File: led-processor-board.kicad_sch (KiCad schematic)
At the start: 66 parts, among them J1 10103594-0001LF, J2 SPARE, J3 SWD, SW1 434133025816, SW2 434133025816, U1 RP2350B, U2 NCP1117ST33T3G, U3 W25Q128JVSIQ, U4 APS6404L-3SQR-SN, U5 RM2, U6 DS3231SN, X1 12MHz

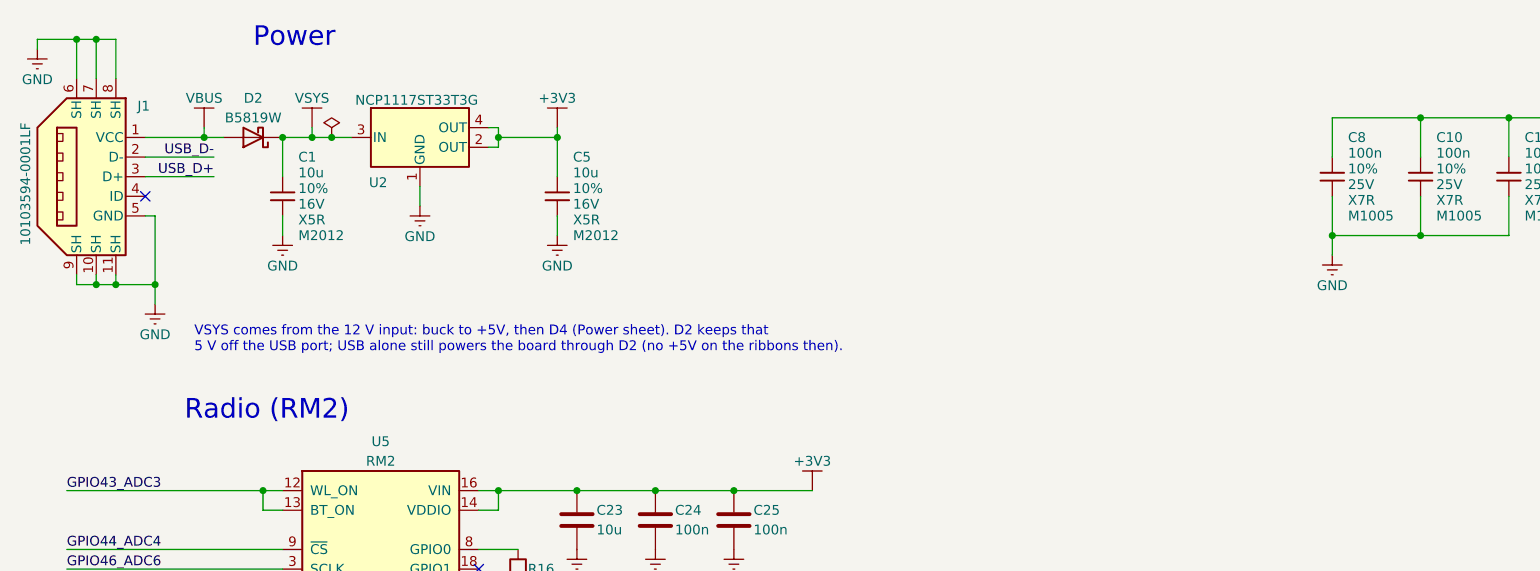
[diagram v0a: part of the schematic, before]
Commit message: Use a USB-C receptacle instead of the micro-B
J1 is now a Korean Hroparts TYPE-C-31-M-12 (LCSC C165948, stock KiCad
footprint), USB 2.0: D+/D- from both sides joined, 5.1k pull-downs on
CC1/CC2 (R56, R57), SBU unconnected, shell to GND. VBUS still feeds D2.
PWR_FLAGs on VBUS and GND replace the drive the old symbol's power pins
gave; ERC is unchanged (only Pi's inherited items).

Co-Authored-By: Claude Opus 5.5 (1M context) <noreply@anthropic.com>
Claude-Session: https://claude.ai/code/session_01CYnkeL97vxsPSCyXSKGro9
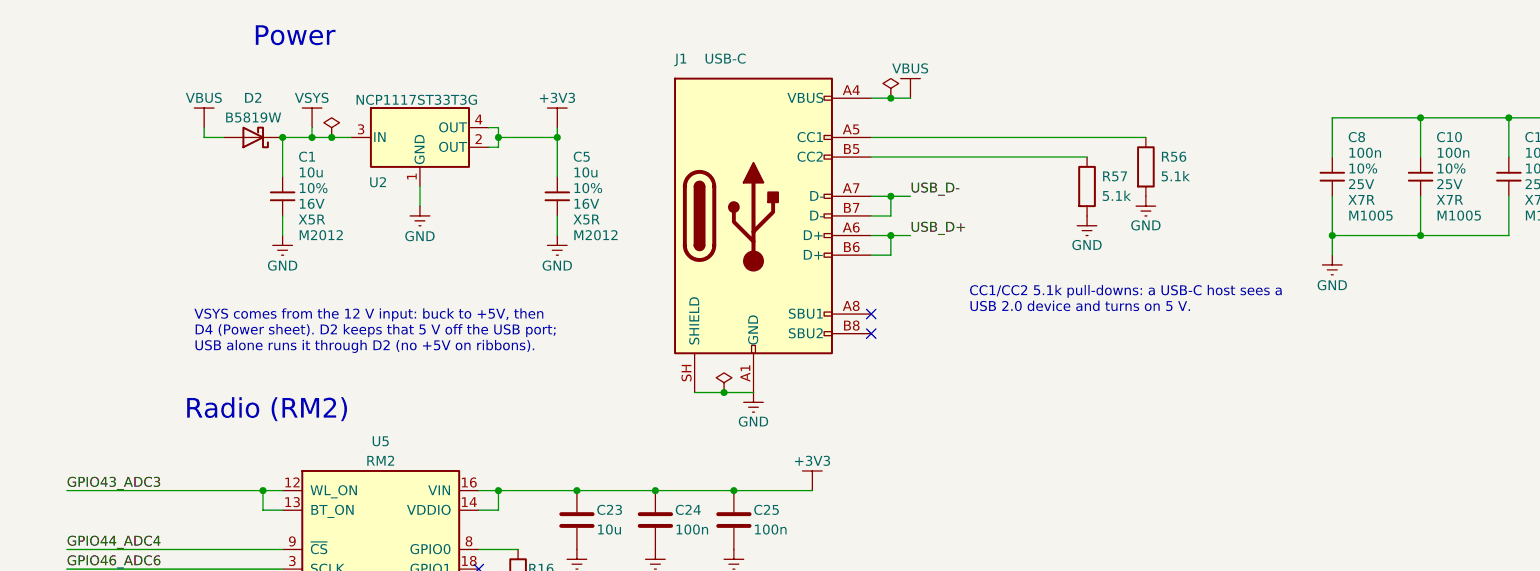
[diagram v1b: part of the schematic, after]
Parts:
- removed J1: 10103594-0001LF, RPI_COMPILED:amphenol_10103594-0001lf, symbol RPI_DB:Connectors | USB/RP-019A1P-1JAX7V
- added J1: USB-C, Connector_USB:USB_C_Receptacle_HRO_TYPE-C-31-M-12, symbol Connector:USB_C_Receptacle_USB2.0_16P
- added R56, R57: 5.1k, Resistor_SMD:R_0402_1005Metric, symbol Device:R
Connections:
- net GND: now also J1.A1 (GND), J1.A12 (GND), J1.B1 (GND), J1.B12 (GND), J1.SH (SHIELD), R56.2, R57.2
- net USB_D+: now also J1.A6 (D+), J1.B6 (D+)
- net USB_D-: now also J1.A7 (D-), J1.B7 (D-)
- net VBUS: now also J1.A4 (VBUS), J1.A9 (VBUS), J1.B4 (VBUS), J1.B9 (VBUS)
- new net: J1.A5 (CC1), R56.1
- new net: J1.B5 (CC2), R57.1
- no-connect marks 8 -> 9
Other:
- note added: "CC1/CC2 5.1k pull-downs: a USB-C host sees a USB 2.0 device and turns on 5 V."
- note added: "VSYS comes from the 12 V input: buck to +5V, then D4 (Power sheet). D2 keeps that 5 V off the USB port; USB alone runs it through D2 (no +5V on ribbons)."
- note removed: "VSYS comes from the 12 V input: buck to +5V, then D4 (Power sheet). D2 keeps that 5 V off the USB port; USB alone still powers the board through D2 (no +5V on the ribbons then)."

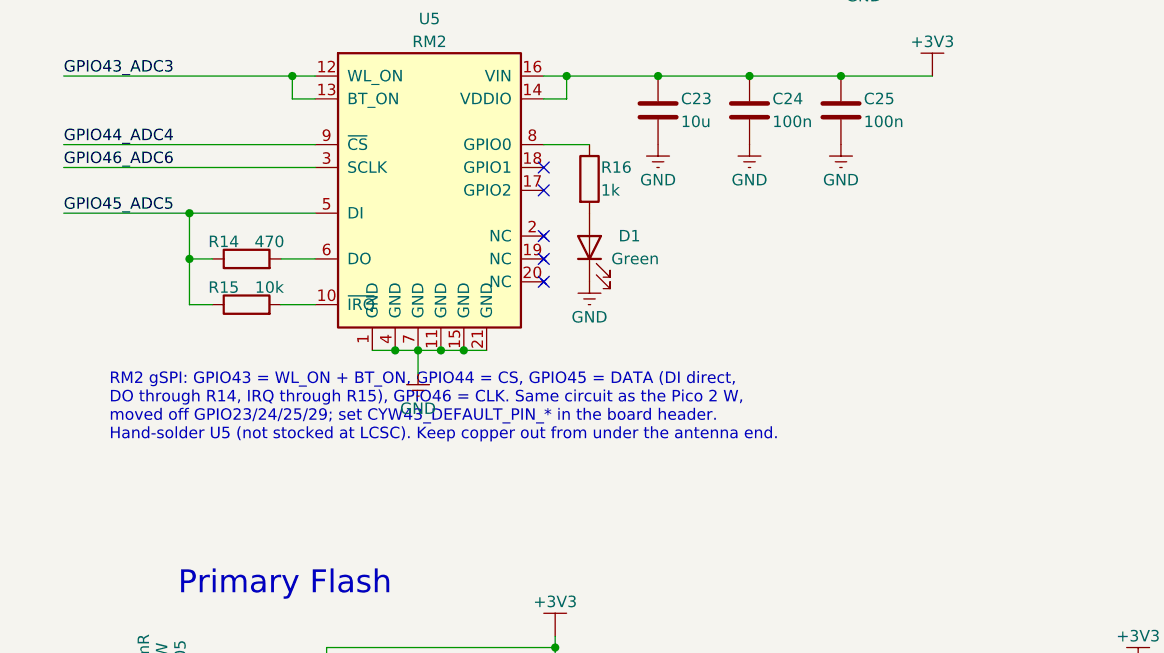
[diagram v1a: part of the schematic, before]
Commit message: Bottom shrouds to the edge; add J9 for the RM2's spare GPIOs
J7/J8 move down until their bottom pins sit just above the antenna
strip, like the left-edge shrouds; J8 also shifts 1.6 mm left to clear
the corner hole. Their 3V3/5V runs are hand-routed through the channel
between the pin rows (one net per layer) and the caps sit above the
shrouds' right ends. This replaces the old OUT4 3V3 run along the
bottom edge into the radio's 3V3 pour.

J9 (1x3: WL_GPIO1, WL_GPIO2, GND) breaks out the CYW43's two unused
GPIOs beside the RM2, in the schematic and on the board; C23/C24 move
up to make room. DRC with schematic parity is clean apart from the
inherited warnings.

Co-Authored-By: Claude Opus 5.5 (1M context) <noreply@anthropic.com>
Claude-Session: https://claude.ai/code/session_01CYnkeL97vxsPSCyXSKGro9
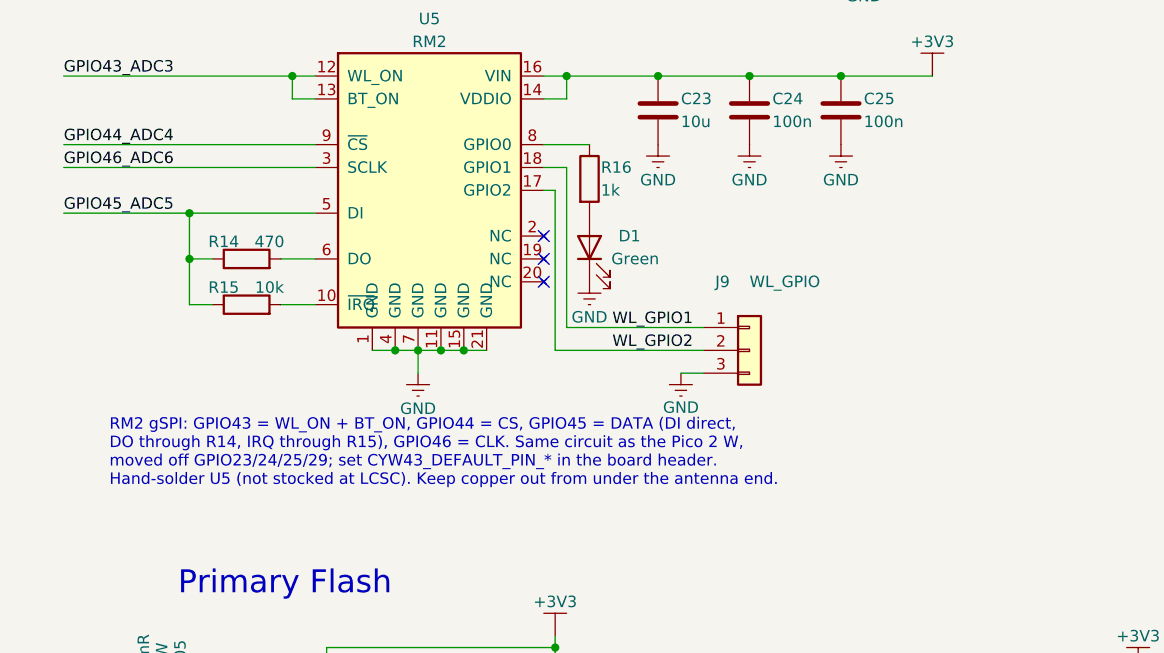
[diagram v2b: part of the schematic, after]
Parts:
- added J9: WL_GPIO, Connector_PinHeader_2.54mm:PinHeader_1x03_P2.54mm_Vertical, symbol Connector_Generic:Conn_01x03
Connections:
- net GND: now also J9.3 (Pin_3)
- net WL_GPIO2: now reaches U5.17 (GPIO2)
- net WL_GPIO2: now also J9.2 (Pin_2)
- net WL_GPIO1: now reaches U5.18 (GPIO1)
- net WL_GPIO1: now also J9.1 (Pin_1)
- no-connect marks 9 -> 7

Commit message: LCSC buttons, and JLCPCB files for SMD-only assembly
SW1/SW2 become the XKB TS-1088R-02526 (LCSC C455281) in Pi's spots, with
the schematic symbols swapped to Switch:SW_Push. tools/jlc.py writes fab/:
gerbers + drill zip, and a BOM and CPL with only the SMD parts JLC places.
The RM2, battery holder, headers, shrouds and J4 are left to hand-solder.

Co-Authored-By: Claude Opus 5.5 (1M context) <noreply@anthropic.com>
Claude-Session: https://claude.ai/code/session_01CYnkeL97vxsPSCyXSKGro9
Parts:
- SW1, SW2: value 434133025816 -> TS-1088R-02526; footprint RPI_COMPILED:wurthelek_434133025816 -> Button_Switch_SMD:SW_SPST_TS-1088-xR025; symbol RPI_DB:Electromechanical | Switches | Tactile/RP-01H0MT-6E9H8F -> Switch:SW_Push; LCSC (none) -> C455281; manufacturer Wurth Elektronik -> XKB Connection; manufacturer_pn 434133025816 -> TS-1088R-02526; package 4.2x3.2x2.5mm -> 4x3x2.5mm; packaging 330mm dia. tape & reel -> (none); packaging_qty 2900 -> (none); part_uid RP-01H0MT-6E9H8F -> (none); size 4.2x3.2x2.5mm -> 4x3x2.5mm
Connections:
- net GND: no longer SW1.2
- net RUN: now also SW2.2; no longer SW2.3, SW2.4
- net ~{USB_BOOT}: now also SW1.2; no longer SW1.3, SW1.4
- net at R4.1, SW2.1: no longer SW2.2
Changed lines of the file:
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@@
 	)
 	(junction
-		(at 265.43 246.38)
-		(diameter 0)
-		(color 0 0 0 0)
-	)
-	(junction
 		(at 304.8 25.4)
 		(diameter 0)
@@
 	)
 	(junction
-		(at 20.32 180.34)
-		(diameter 0)
-		(color 0 0 0 0)
-	)
-	(junction
 		(at 36.83 152.4)
 		(diameter 0)
@@
 	)
 	(junction
-		(at 250.19 246.38)
-		(diameter 0)
-		(color 0 0 0 0)
-	)
-	(junction
 		(at 236.22 101.6)
 		(diameter 0)
@@
 	)
 	(junction
-		(at 20.32 195.58)
-		(diameter 0)
-		(color 0 0 0 0)
-	)
-	(junction
 		(at 207.01 101.6)
 		(diameter 0)
@@
 	(wire
 		(pts
-			(xy 251.46 248.92) (xy 250.19 248.92)
-		)
-		(stroke
-			(width 0)
-			(type default)
-		)
-	)
-	(wire
-		(pts
 			(xy 265.43 129.54) (xy 245.11 129.54)
 		)
@@
 	(wire
 		(pts
-			(xy 265.43 246.38) (xy 264.16 246.38)
+			(xy 265.43 246.38) (xy 262.89 246.38)
 		)
 		(stroke
@@
 	(wire
 		(pts
-			(xy 22.86 180.34) (xy 20.32 180.34)
-		)
-		(stroke
-			(width 0)
-			(type default)
-		)
-	)
-	(wire
-		(pts
 			(xy 49.53 83.82) (xy 21.59 83.82)
 		)
@@
 	(wire
 		(pts
-			(xy 251.46 246.38) (xy 250.19 246.38)
+			(xy 252.73 246.38) (xy 250.19 246.38)
 		)
 		(stroke
@@
 	(wire
 		(pts
-			(xy 265.43 248.92) (xy 265.43 246.38)
-		)
-		(stroke
-			(width 0)
-			(type default)
-		)
-	)
-	(wire
-		(pts
 			(xy 38.1 93.98) (xy 35.56 93.98)
 		)
@@
 	(wire
 		(pts
-			(xy 22.86 194.31) (xy 22.86 195.58)
-		)
-		(stroke
-			(width 0)
-			(type default)
-		)
-	)
-	(wire
-		(pts
 			(xy 50.8 137.16) (xy 50.8 140.97)
 		)
@@
 	(wire
 		(pts
-			(xy 22.86 195.58) (xy 20.32 195.58)
-		)
-		(stroke
-			(width 0)
-			(type default)
-		)
-	)
-	(wire
-		(pts
 			(xy 143.51 245.11) (xy 158.75 245.11)
 		)
@@
 	(wire
 		(pts
-			(xy 250.19 248.92) (xy 250.19 246.38)
-		)
-		(stroke
-			(width 0)
-			(type default)
-		)
-	)
-	(wire
-		(pts
 			(xy 208.28 215.9) (xy 208.28 193.04)
 		)
@@
 	(wire
 		(pts
-			(xy 20.32 180.34) (xy 20.32 181.61)
+			(xy 20.32 180.34) (xy 20.32 182.88)
 		)
 		(stroke
@@
 	(wire
 		(pts
-			(xy 22.86 181.61) (xy 22.86 180.34)
-		)
-		(stroke
-			(width 0)
-			(type default)
-		)
-	)
-	(wire
-		(pts
 			(xy 245.11 170.18) (xy 260.35 170.18)
 		)
@@
 	(wire
 		(pts
-			(xy 20.32 194.31) (xy 20.32 195.58)
+			(xy 20.32 193.04) (xy 20.32 195.58)
 		)
 		(stroke
@@
 	(wire
 		(pts
-			(xy 264.16 248.92) (xy 265.43 248.92)
-		)
-		(stroke
-			(width 0)
-			(type default)
-		)
-	)
-	(wire
-		(pts
 			(xy 339.09 40.64) (xy 339.09 41.91)
 		)
@@
 	)
 	(symbol
-		(lib_id "RPI_DB:Electromechanical | Switches | Tactile/RP-01H0MT-6E9H8F")
+		(lib_id "Switch:SW_Push")
 		(at 257.81 246.38 0)
 		(mirror y)
@@
 			)
 		)
-		(property "Value" "434133025816"
+		(property "Value" "TS-1088R-02526"
 			(at 257.81 241.3 0)
 			(show_name no)
@@
 			)
 		)
-		(property "Footprint" "RPI_COMPILED:wurthelek_434133025816"
+		(property "Footprint" "Button_Switch_SMD:SW_SPST_TS-1088-xR025"
 			(at 257.81 241.3 0)
 			(hide yes)
@@
 			)
 		)
-		(property "Datasheet" "file:///C:\\rpi-pdb\\parts\\Electromechanical\\Switches\\Tactile\\WURTHELEK_434133025816\\datasheets"
+		(property "Datasheet" "https://jlcpcb.com/partdetail/XKB_Connection-TS_1088R02526/C455281"
 			(at 257.81 241.3 0)
 			(hide yes)
@@
 			)
 		)
-		(property "Description" "Tactile Pushbutton, SPST, N.O., 4.2x3.2x2.5mm"
+		(property "Description" "Tactile Pushbutton, SPST, N.O., 4x3x2.5mm"
 			(at 257.81 246.38 0)
 			(hide yes)
@@
 			)
 		)
-		(property "part_uid" "RP-01H0MT-6E9H8F"
+		(property "manufacturer" "XKB Connection"
 			(at 257.81 246.38 0)
 			(hide yes)
@@
 			)
 		)
-		(property "manufacturer" "Wurth Elektronik"
+		(property "manufacturer_pn" "TS-1088R-02526"
 			(at 257.81 246.38 0)
 			(hide yes)
@@
 			)
 		)
-		(property "manufacturer_pn" "434133025816"
+		(property "size" "4x3x2.5mm"
 			(at 257.81 246.38 0)
 			(hide yes)
@@
 			)
 		)
-		(property "packaging" "330mm dia. tape & reel"
-			(at 257.81 246.38 0)
-			(hide yes)
-			(show_name no)
-			(do_not_autoplace no)
-			(effects
-				(font
-					(size 1.27 1.27)
-				)
-			)
-		)
-		(property "packaging_qty" "2900"
-			(at 257.81 246.38 0)
-			(hide yes)
-			(show_name no)
-			(do_not_autoplace no)
-			(effects
-				(font
-					(size 1.27 1.27)
-				)
-			)
-		)
-		(property "size" "4.2x3.2x2.5mm"
+		(property "z_height_max" ""
 			(at 257.81 246.38 0)
 			(hide yes)
@@
 			)
 		)
-		(property "z_height_max" ""
+		(property "z_height_nom" "2.5mm"
 			(at 257.81 246.38 0)
 			(hide yes)
@@
 			)
 		)
-		(property "z_height_nom" "2.5mm"
+		(property "package" "4x3x2.5mm"
 			(at 257.81 246.38 0)
 			(hide yes)
@@
 			)
 		)
-		(property "package" "4.2x3.2x2.5mm"
-			(at 257.81 246.38 0)
+		(property "LCSC" "C455281"
+			(at 257.81 241.3 0)
 			(hide yes)
 			(show_name no)
@@
 		(pin "2"
 		)
-		(pin "4"
-		)
-		(pin "3"
-		)
 		(instances
 			(project "led-processor-board"
@@
 	)
 	(symbol
-		(lib_id "RPI_DB:Electromechanical | Switches | Tactile/RP-01H0MT-6E9H8F")
+		(lib_id "Switch:SW_Push")
 		(at 20.32 187.96 90)
 		(unit 1)
@@
 			)
 		)
-		(property "Value" "434133025816"
+		(property "Value" "TS-1088R-02526"
 			(at 23.495 189.2299 90)
 			(show_name no)
@@
 			)
 		)
-		(property "Footprint" "RPI_COMPILED:wurthelek_434133025816"
+		(property "Footprint" "Button_Switch_SMD:SW_SPST_TS-1088-xR025"
 			(at 15.24 187.96 0)
 			(hide yes)
@@
 			)
 		)
-		(property "Datasheet" "file:///C:\\rpi-pdb\\parts\\Electromechanical\\Switches\\Tactile\\WURTHELEK_434133025816\\datasheets"
+		(property "Datasheet" "https://jlcpcb.com/partdetail/XKB_Connection-TS_1088R02526/C455281"
 			(at 15.24 187.96 0)
 			(hide yes)
@@
 			)
 		)
-		(property "Description" "Tactile Pushbutton, SPST, N.O., 4.2x3.2x2.5mm"
-			(at 20.32 187.96 0)
-			(hide yes)
-			(show_name no)
-			(do_not_autoplace no)
-			(effects
-				(font
-					(size 1.27 1.27)
-				)
-			)
-		)
-		(property "part_uid" "RP-01H0MT-6E9H8F"
+		(property "Description" "Tactile Pushbutton, SPST, N.O., 4x3x2.5mm"
 			(at 20.32 187.96 0)
 			(hide yes)
@@
 			)
 		)
-		(property "manufacturer" "Wurth Elektronik"
+		(property "manufacturer" "XKB Connection"
 			(at 20.32 187.96 0)
 			(hide yes)
@@
 			)
 		)
-		(property "manufacturer_pn" "434133025816"
+		(property "manufacturer_pn" "TS-1088R-02526"
 			(at 20.32 187.96 0)
 			(hide yes)
@@
 			)
 		)
-		(property "packaging" "330mm dia. tape & reel"
+		(property "size" "4x3x2.5mm"
 			(at 20.32 187.96 0)
 			(hide yes)
@@
 			)
 		)
-		(property "packaging_qty" "2900"
-			(at 20.32 187.96 0)
-			(hide yes)
-			(show_name no)
-			(do_not_autoplace no)
-			(effects
-				(font
-					(size 1.27 1.27)
-				)
-			)
-		)
-		(property "size" "4.2x3.2x2.5mm"
+		(property "z_height_max" ""
 			(at 20.32 187.96 0)
 			(hide yes)
@@
 			)
 		)
-		(property "z_height_max" ""
+		(property "z_height_nom" "2.5mm"
 			(at 20.32 187.96 0)
 			(hide yes)
@@
 			)
 		)
-		(property "z_height_nom" "2.5mm"
+		(property "package" "4x3x2.5mm"
 			(at 20.32 187.96 0)
 			(hide yes)
@@
 			)
 		)
-		(property "package" "4.2x3.2x2.5mm"
-			(at 20.32 187.96 0)
+		(property "LCSC" "C455281"
+			(at 15.24 187.96 0)
 			(hide yes)
 			(show_name no)
@@
 		(pin "2"
 		)
-		(pin "3"
-		)
-		(pin "4"
-		)
 		(instances

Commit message: Remove R9 and the dead GPIO0 branch to it
R9 is Pi's unfitted 0R option from GPIO0 to the flash chip select. It was
DNP here too, so its only effect was a stub on OUT1's first data line.
Dropped from the schematic and board with its wiring; JLC files and
previews regenerated (assembly BOM/CPL unchanged).

Co-Authored-By: Claude Opus 5.5 (1M context) <noreply@anthropic.com>
Claude-Session: https://claude.ai/code/session_01CYnkeL97vxsPSCyXSKGro9
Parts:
- removed R9: 0, RPI_COMPILED:generic_resc1005x35, symbol RPI_DB:Resistors | Chip | M1005/RP-019A1P-4Y4V63
